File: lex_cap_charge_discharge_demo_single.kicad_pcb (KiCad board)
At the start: 2 copper layers, 30 x 40.4 mm, 12 parts, among them J1 +5V, J2 GND, SW1 charge, SW2 discharge

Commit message: Add optional component (with header) around cap
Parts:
- added J3: Conn_01x01_Socket, Connector_PinSocket_2.54mm:PinSocket_1x01_P2.54mm_Vertical, F.Cu at (68.4, 70.4)
- added J4: Conn_01x01_Socket, Connector_PinSocket_2.54mm:PinSocket_1x01_P2.54mm_Vertical, F.Cu at (68.4, 62.7)
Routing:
- net Net-(J3-Pin_1): track 37.3 -> 42.5 mm
- net GND: track 15.0 -> 20.3 mm

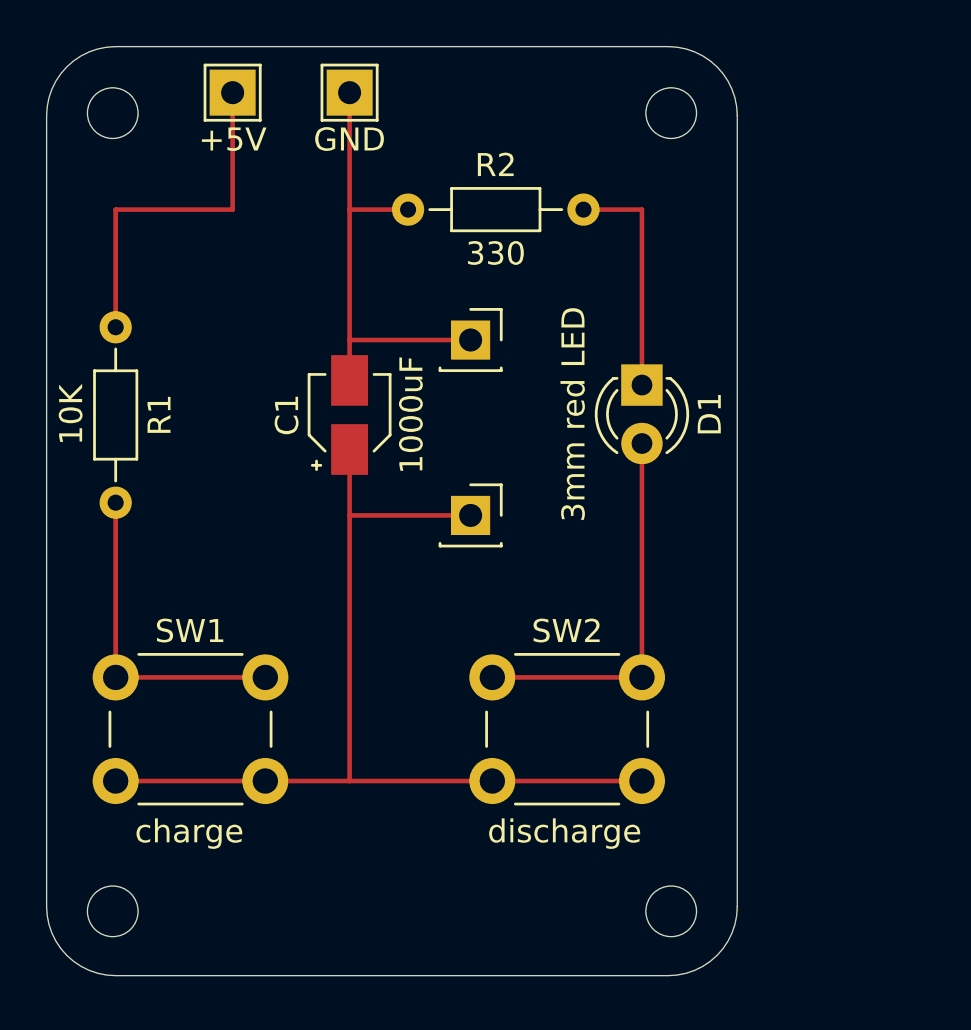
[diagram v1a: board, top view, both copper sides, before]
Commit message: Add optional text at header points for it
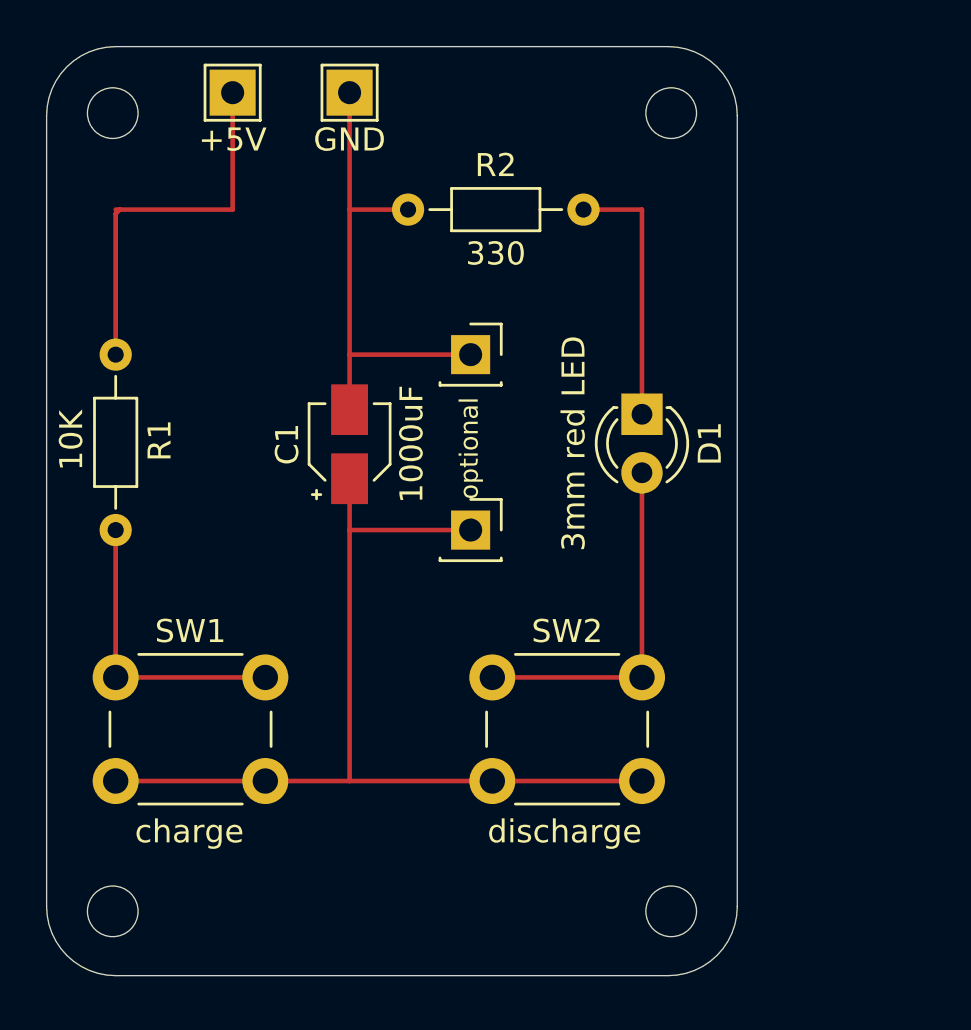
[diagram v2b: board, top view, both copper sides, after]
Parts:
- moved C1 1.27 mm to (63.2, 67.3)
- moved D1 1.27 mm to (75.9, 66.0)
- moved R1 1.19 mm to (53.0, 63.4)
- moved J3 0.64 mm to (68.4, 71.0)
- moved J4 0.63 mm to (68.4, 63.4)
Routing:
- net Net-(D1-A): track 16.7 -> 15.4 mm
- net Net-(J3-Pin_1): track 42.5 -> 41.2 mm
- net Net-(D1-K): track 10.2 -> 11.4 mm
- net GND: track 20.3 -> 21.6 mm
- net +5V: track 15.3 -> 16.5 mm
- net Net-(SW1-A): track 14.1 -> 12.9 mm
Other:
- board text added: "optional"
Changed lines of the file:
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@@
 	(footprint "Resistor_THT:R_Axial_DIN0204_L3.6mm_D1.6mm_P7.62mm_Horizontal"
 		(layer "F.Cu")
-		(at 53 62.19 -90)
+		(at 53 63.3792 -90)
 		(descr "Resistor, Axial_DIN0204 series, Axial, Horizontal, pin pitch=7.62mm, 0.167W, length*diameter=3.6*1.6mm^2, http://cdn-reichelt.de/documents/datenblatt/B400/1_4W%23YAG.pdf")
 		(tags "Resistor Axial_DIN0204 series Axial Horizontal pin pitch 7.62mm 0.167W length 3.6mm diameter 1.6mm")
 		(property "Reference" "R1"
-			(at 3.81 -1.92 90)
+			(at 3.7292 -1.92 90)
 			(layer "F.SilkS")
 			(effects
@@
 		)
 		(property "Value" "10K"
-			(at 3.81 1.92 90)
+			(at 3.7292 1.92 90)
 			(layer "F.SilkS")
 			(effects
@@
 		)
 		(fp_text user "${REFERENCE}"
-			(at 3.81 0 90)
+			(at 5.08 0 90)
 			(layer "F.Fab")
 			(effects
@@
 	(footprint "Connector_PinSocket_2.54mm:PinSocket_1x01_P2.54mm_Vertical"
 		(layer "F.Cu")
-		(at 68.4178 70.3642)
+		(at 68.4178 70.9992)
 		(descr "Through hole straight socket strip, 1x01, 2.54mm pitch, single row (from Kicad 4.0.7), script generated")
 		(tags "Through hole socket strip THT 1x01 2.54mm single row")
@@
 			(at 0 2.77 0)
 			(layer "F.Fab")
+			(hide yes)
 			(effects
 				(font
@@
 		(sheetname "/")
 		(sheetfile "lex_cap_charge_discharge_demo_single.kicad_sch")
-		(attr through_hole)
+		(attr through_hole exclude_from_pos_files exclude_from_bom dnp)
 		(fp_line
 			(start -1.33 1.21)
@@
 	(footprint "Capacitor_SMD:CP_Elec_3x5.3"
 		(layer "F.Cu")
-		(at 63.16 66 90)
+		(at 63.16 67.27 90)
 		(descr "SMT capacitor, aluminium electrolytic, 3x5.3, Cornell Dubilier Electronics ")
 		(tags "Capacitor Electrolytic")
@@
 	(footprint "LED_THT:LED_D3.0mm"
 		(layer "F.Cu")
-		(at 75.86 64.7 -90)
+		(at 75.86 65.97 -90)
 		(descr "LED, diameter 3.0mm, 2 pins, generated by kicad-footprint-generator")
 		(tags "LED")
@@
 	(footprint "Connector_PinSocket_2.54mm:PinSocket_1x01_P2.54mm_Vertical"
 		(layer "F.Cu")
-		(at 68.4178 62.7442)
+		(at 68.4178 63.3792)
 		(descr "Through hole straight socket strip, 1x01, 2.54mm pitch, single row (from Kicad 4.0.7), script generated")
 		(tags "Through hole socket strip THT 1x01 2.54mm single row")
@@
 		(sheetname "/")
 		(sheetfile "lex_cap_charge_discharge_demo_single.kicad_sch")
-		(attr through_hole)
+		(attr through_hole exclude_from_pos_files exclude_from_bom dnp)
 		(fp_line
 			(start -1.33 1.21)
@@
 		)
 		(layer "Edge.Cuts")
+	)
+	(gr_text "optional"
+		(at 68.8242 69.6692 90)
+		(layer "F.SilkS")
+		(effects
+			(font
+				(size 0.8 0.8)
+				(thickness 0.1)
+			)
+			(justify left bottom)
+		)
 	)
 	(gr_text_box "cap-fun v1.0"
@@
 	)
 	(segment
+		(start 53 70.9992)
+		(end 53 77.4)
+		(width 0.2)
+		(layer "F.Cu")
+		(net 1)
+	)
+	(segment
 		(start 53 77.4)
 		(end 59.5 77.4)
@@
 	)
 	(segment
-		(start 53 69.81)
-		(end 53 77.4)
+		(start 63.16 70.9992)
+		(end 63.16 81.9)
 		(width 0.2)
 		(layer "F.Cu")
-		(net 1)
+		(net 2)
 	)
 	(segment
-		(start 68.4178 70.3642)
-		(end 63.16 70.3642)
+		(start 68.4178 70.9992)
+		(end 63.16 70.9992)
+		(width 0.2)
+		(layer "F.Cu")
+		(net 2)
+	)
+	(segment
+		(start 63.16 68.77)
+		(end 63.16 70.9992)
 		(width 0.2)
 		(layer "F.Cu")
@@
 	)
 	(segment
-		(start 63.16 67.5)
-		(end 63.16 70.3642)
-		(width 0.2)
-		(layer "F.Cu")
-		(net 2)
-	)
-	(segment
-		(start 63.16 70.3642)
-		(end 63.16 81.9)
-		(width 0.2)
-		(layer "F.Cu")
-		(net 2)
-	)
-	(segment
 		(start 59.5 81.9)
 		(end 63.16 81.9)
@@
 	)
 	(segment
-		(start 75.86 64.7)
-		(end 75.86 57.08)
+		(start 75.86 57.08)
+		(end 75.86 65.97)
 		(width 0.2)
 		(layer "F.Cu")
 		(net 3)
+	)
+	(segment
+		(start 75.86 68.51)
+		(end 75.86 77.4)
+		(width 0.2)
+		(layer "F.Cu")
+		(net 4)
 	)
 	(segment
@@
 	)
 	(segment
-		(start 75.86 77.4)
-		(end 75.86 67.24)
-		(width 0.2)
-		(layer "F.Cu")
-		(net 4)
-	)
-	(segment
-		(start 68.4178 62.7442)
-		(end 63.16 62.7442)
-		(width 0.2)
-		(layer "F.Cu")
-		(net 5)
-	)
-	(segment
-		(start 63.16 62.7442)
-		(end 63.16 64.5)
-		(width 0.2)
-		(layer "F.Cu")
-		(net 5)
-	)
-	(segment
-		(start 63.16 57.08)
-		(end 63.16 62.7442)
+		(start 63.16 65.77)
+		(end 63.16 63.3792)
 		(width 0.2)
 		(layer "F.Cu")
@@
 	)
 	(segment
+		(start 68.4178 63.3792)
+		(end 63.16 63.3792)
+		(width 0.2)
+		(layer "F.Cu")
+		(net 5)
+	)
+	(segment
 		(start 65.7 57.08)
 		(end 63.16 57.08)
@@
 	)
 	(segment
+		(start 63.16 63.3792)
+		(end 63.16 57.08)
+		(width 0.2)
+		(layer "F.Cu")
+		(net 5)
+	)
+	(segment
 		(start 58.08 57.08)
-		(end 53 57.08)
+		(end 53.1778 57.08)
+		(width 0.2)
+		(layer "F.Cu")
+		(net 6)
+	)
+	(segment
+		(start 53 57.2578)
+		(end 53 63.3792)
 		(width 0.2)
 		(layer "F.Cu")
@@
 	)
 	(segment
-		(start 53 57.08)
-		(end 53 62.19)
+		(start 53.1778 57.08)
+		(end 53 57.2578)
 		(width 0.2)
 		(layer "F.Cu")
+		(net 6)
+	)
+	(segment
+		(start 53.1778 57.08)
+		(end 53 57.08)
+		(width 0.2)
+		(layer "F.Cu")

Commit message: Make board bigger (4cm x 4cm), fix SMD cap to THT
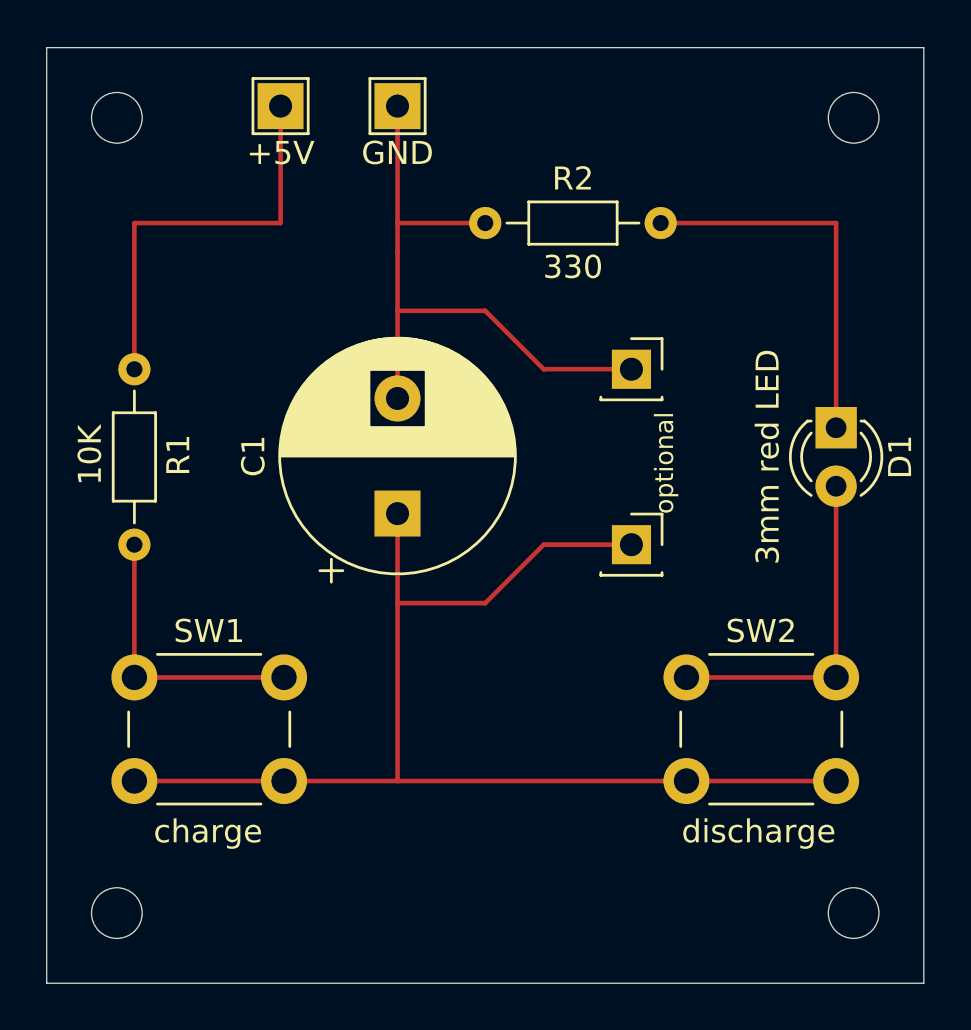
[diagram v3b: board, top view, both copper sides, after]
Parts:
- C1: footprint Capacitor_SMD:CP_Elec_3x5.3 -> Capacitor_THT:CP_Radial_D10.0mm_P5.00mm
- moved D1 8.45 mm to (84.3, 66.6)
- moved SW2 8.43 mm to (77.8, 77.4)
- moved H4 7.93 mm to (85.1, 53.1)
- moved H2 7.93 mm to (85.1, 87.6)
- moved J3 7.01 mm to (75.4, 71.6)
- moved J4 7.01 mm to (75.4, 64.0)
- moved C1 3.66 mm to (65.2, 70.3)
- moved R2 3.40 mm to (69.1, 57.7)
- moved J2 2.16 mm to (65.2, 52.6)
- moved J1 2.16 mm to (60.2, 52.6)
- moved R1 1.03 mm to (53.8, 64.0)
- moved SW1 0.81 mm to (53.8, 77.4)
- moved H3 0.27 mm to (53.1, 53.1)
- moved H1 0.19 mm to (53.1, 87.6)
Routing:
- net Net-(J3-Pin_1): track 41.2 -> 53.3 mm
- net GND: track 21.6 -> 27.7 mm
- net Net-(D1-K): track 11.4 -> 16.5 mm
- net +5V: track 16.5 -> 17.8 mm
- net Net-(SW1-A): track 12.9 -> 12.3 mm
- net Net-(D1-A): track 15.4 -> 14.8 mm
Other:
- board size 30 x 40.4 mm -> 38.1 x 40.6 mm
